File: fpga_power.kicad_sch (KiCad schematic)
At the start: 77 parts, among them U2 XC7A50T-FGG484, U3 LP3878MR-ADJ, U4 LP3878MR-ADJ, U5 LP3878MR-ADJ, U6 LP3878MR-ADJ, U7 LP3878MR-ADJ, U8 MCP23008-E/ML

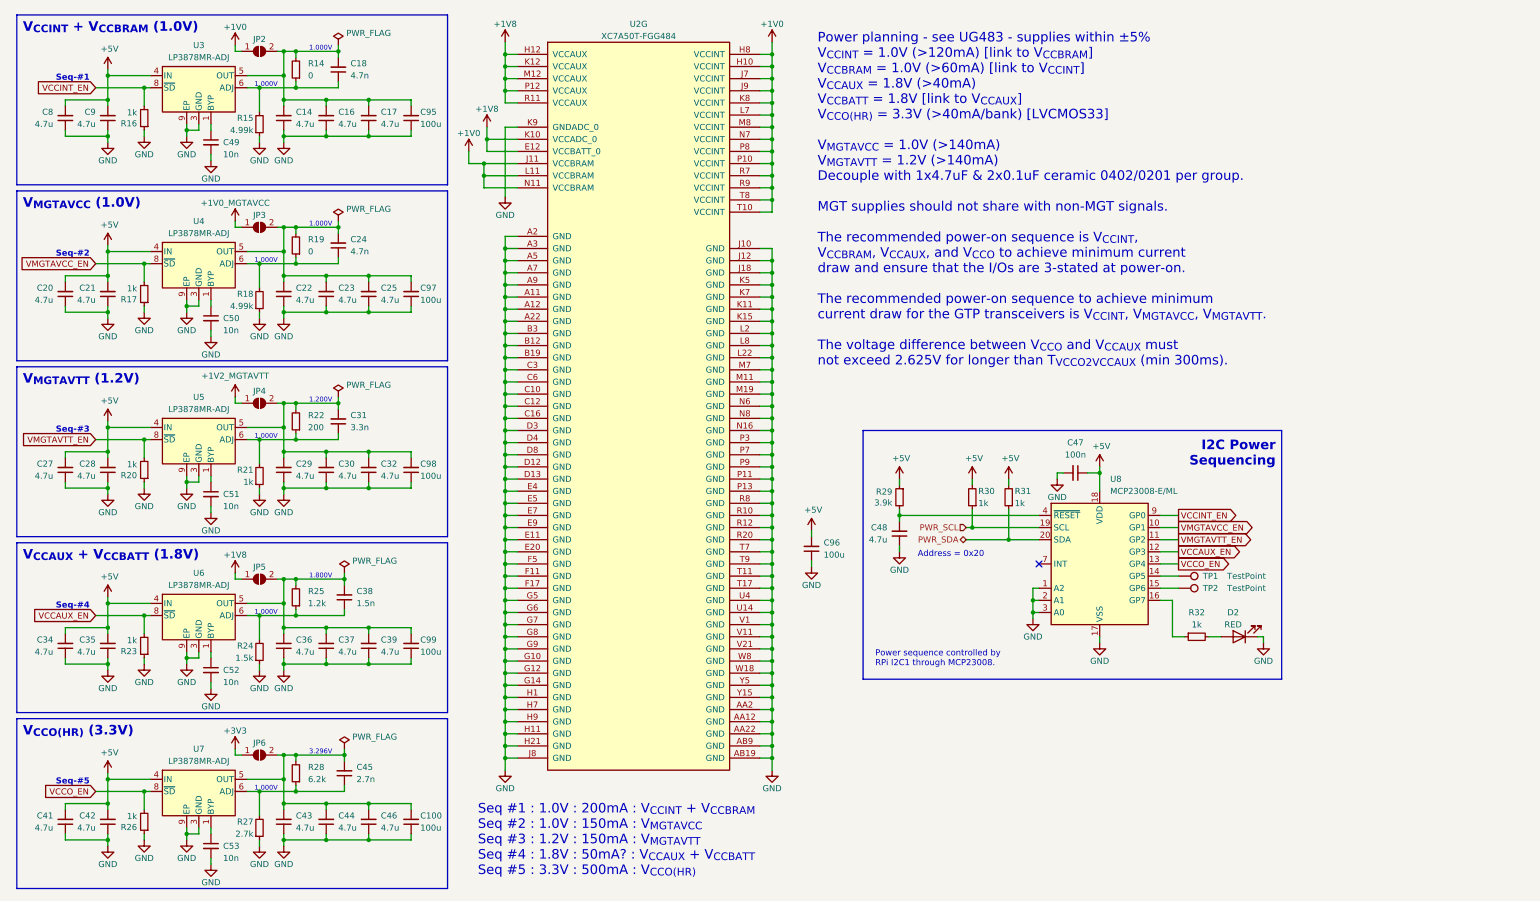
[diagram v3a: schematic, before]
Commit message: Changed linear PSU for SMPS and a few other changes
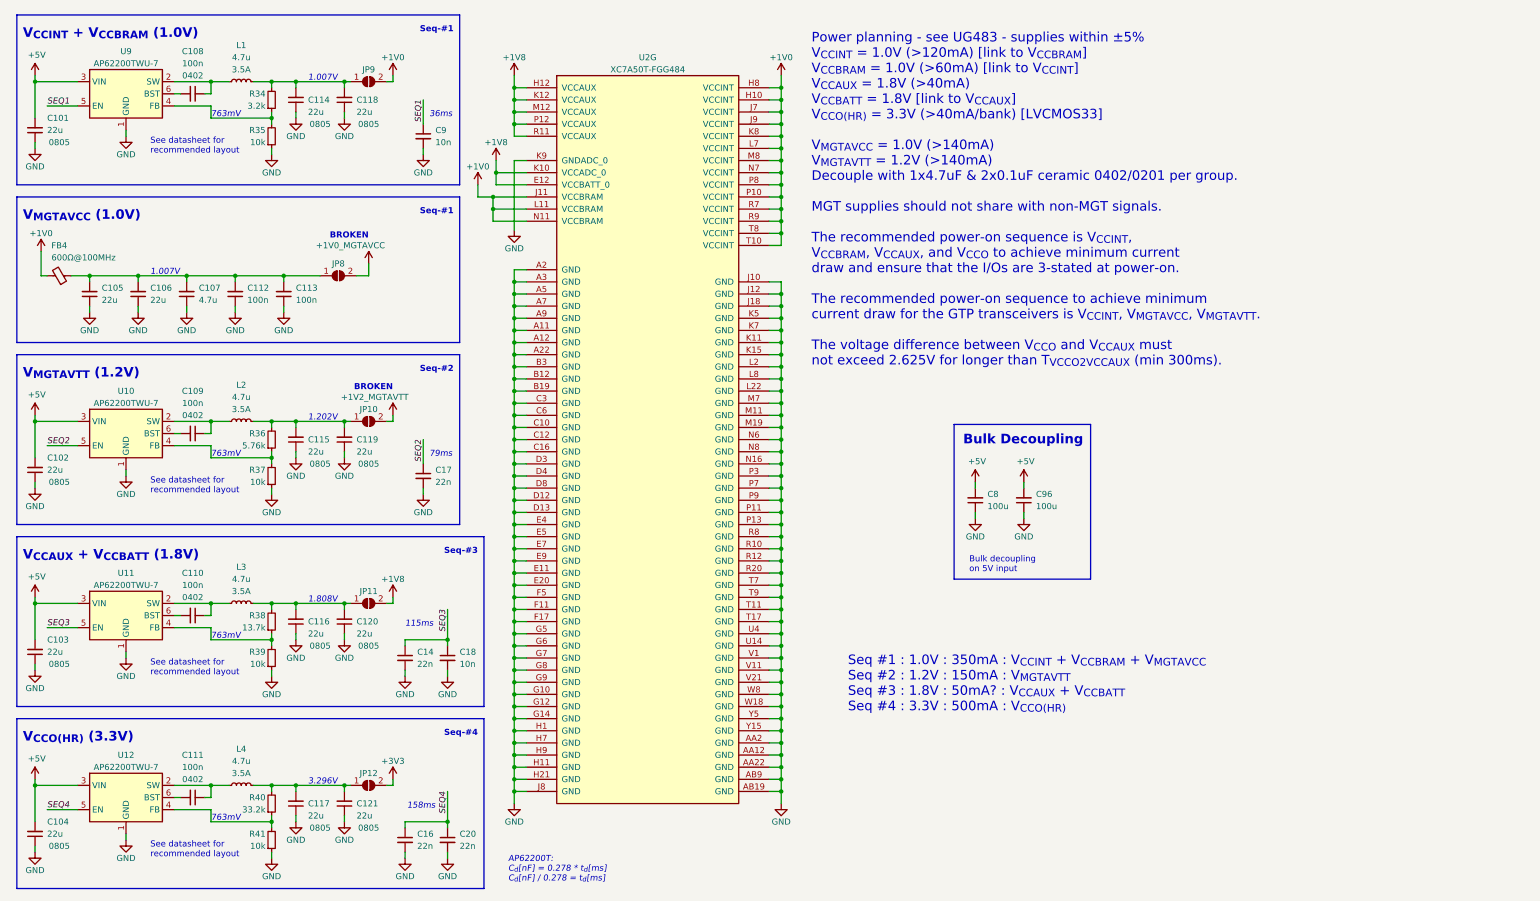
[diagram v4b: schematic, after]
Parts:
- removed C100, C95, C97, C98, C99: 100u, Capacitor_SMD:C_1206_3216Metric_Pad1.33x1.80mm_HandSolder, symbol Device:C_Small
- removed C21, C22, C23, C25, C27, C28, C29, C30, C32, C34, C35, C36, C37, C39, C41, C42, C43, C44, C46, C48: 4.7u, Capacitor_SMD:C_0402_1005Metric_Pad0.74x0.62mm_HandSolder, symbol Device:C_Small
- removed C24: 4.7n, Capacitor_SMD:C_0402_1005Metric_Pad0.74x0.62mm_HandSolder, symbol Device:C_Small
- removed C31: 3.3n, Capacitor_SMD:C_0402_1005Metric_Pad0.74x0.62mm_HandSolder, symbol Device:C_Small
- removed C38: 1.5n, Capacitor_SMD:C_0402_1005Metric_Pad0.74x0.62mm_HandSolder, symbol Device:C_Small
- removed C45: 2.7n, Capacitor_SMD:C_0402_1005Metric_Pad0.74x0.62mm_HandSolder, symbol Device:C_Small
- removed C47: 100n, Capacitor_SMD:C_0402_1005Metric_Pad0.74x0.62mm_HandSolder, symbol Device:C_Small
- removed C49, C50, C51, C52, C53: 10n, Capacitor_SMD:C_0402_1005Metric_Pad0.74x0.62mm_HandSolder, symbol Device:C_Small
- removed D2: RED, LED_SMD:LED_0603_1608Metric_Pad1.05x0.95mm_HandSolder, symbol Device:LED
- removed JP2, JP3, JP4, JP5, JP6: ID_WP, Jumper:SolderJumper-2_P1.3mm_Open_TrianglePad1.0x1.5mm, symbol Jumper:SolderJumper_2_Open
- removed R14, R19: 0, Resistor_SMD:R_0402_1005Metric_Pad0.72x0.64mm_HandSolder, symbol Device:R_Small
- removed R15, R18: 4.99k, Resistor_SMD:R_0402_1005Metric_Pad0.72x0.64mm_HandSolder, symbol Device:R_Small
- removed R16, R17, R20, R21, R23, R26, R30, R31, R32: 1k, Resistor_SMD:R_0402_1005Metric_Pad0.72x0.64mm_HandSolder, symbol Device:R_Small
- removed R22: 200, Resistor_SMD:R_0402_1005Metric_Pad0.72x0.64mm_HandSolder, symbol Device:R_Small
- removed R24: 1.5k, Resistor_SMD:R_0402_1005Metric_Pad0.72x0.64mm_HandSolder, symbol Device:R_Small
- removed R25: 1.2k, Resistor_SMD:R_0402_1005Metric_Pad0.72x0.64mm_HandSolder, symbol Device:R_Small
- removed R27: 2.7k, Resistor_SMD:R_0402_1005Metric_Pad0.72x0.64mm_HandSolder, symbol Device:R_Small
- removed R28: 6.2k, Resistor_SMD:R_0402_1005Metric_Pad0.72x0.64mm_HandSolder, symbol Device:R_Small
- removed R29: 3.9k, Resistor_SMD:R_0402_1005Metric_Pad0.72x0.64mm_HandSolder, symbol Device:R_Small
- removed TP1, TP2: TestPoint, TestPoint:TestPoint_Pad_D1.0mm, symbol Connector:TestPoint
- removed U3, U4, U5, U6, U7: LP3878MR-ADJ, Package_SO:TI_SO-PowerPAD-8, symbol LP3878SD-ADJ:LP3878SD-ADJ
- removed U8: MCP23008-E/ML, Package_DFN_QFN:QFN-20-1EP_4x4mm_P0.5mm_EP2.7x2.7mm, symbol Interface_Expansion:MCP23008-xML
- added C101, C102, C103, C104, C105, C106, C114, C115, C116, C117, C118, C119, C120, C121: 22u, Capacitor_SMD:C_0805_2012Metric, symbol Device:C_Small
- added C107: 4.7u, Capacitor_SMD:C_0402_1005Metric_Pad0.74x0.62mm_HandSolder, symbol Device:C_Small
- added C108, C109, C110, C111: 100n, Capacitor_SMD:C_0402_1005Metric, symbol Device:C_Small
- added C112, C113: 100n, Capacitor_SMD:C_0402_1005Metric_Pad0.74x0.62mm_HandSolder, symbol Device:C_Small
- added FB4: 600Ω@100MHz, Inductor_SMD:L_0603_1608Metric_Pad1.05x0.95mm_HandSolder, symbol Device:FerriteBead_Small
- added JP10, JP11, JP12, JP8, JP9: ID_WP, Jumper:SolderJumper-2_P1.3mm_Open_TrianglePad1.0x1.5mm, symbol Jumper:SolderJumper_2_Open
- added L1, L2, L3, L4: 4.7u, Inductor_SMD:L_Chilisin_BMRB00050518, symbol Device:L_Small
- added R34: 3.2k, Resistor_SMD:R_0402_1005Metric, symbol Device:R_Small
- added R35, R37, R39, R41: 10k, Resistor_SMD:R_0402_1005Metric, symbol Device:R_Small
- added R36: 5.76k, Resistor_SMD:R_0402_1005Metric, symbol Device:R_Small
- added R38: 13.7k, Resistor_SMD:R_0402_1005Metric, symbol Device:R_Small
- added R40: 33.2k, Resistor_SMD:R_0402_1005Metric, symbol Device:R_Small
- added U10, U11, U12, U9: AP62200TWU-7, Package_TO_SOT_SMD:TSOT-23-6, symbol Diodes-Incorporated-AP62200:AP62200TWU-7
- C14, C16, C17, C20: value 4.7u -> 22n; footprint Capacitor_SMD:C_0402_1005Metric_Pad0.74x0.62mm_HandSolder -> Capacitor_SMD:C_0402_1005Metric; LCSC C23733 -> C1532; Pkg (none) -> 0402
- C18: value 4.7n -> 10n; footprint Capacitor_SMD:C_0402_1005Metric_Pad0.74x0.62mm_HandSolder -> Capacitor_SMD:C_0402_1005Metric; LCSC C1538 -> C15195; Pkg (none) -> 0402
- C8: value 4.7u -> 100u; footprint Capacitor_SMD:C_0402_1005Metric_Pad0.74x0.62mm_HandSolder -> Capacitor_SMD:C_1206_3216Metric_Pad1.33x1.80mm_HandSolder; LCSC C23733 -> C15008
- C9: value 4.7u -> 10n; footprint Capacitor_SMD:C_0402_1005Metric_Pad0.74x0.62mm_HandSolder -> Capacitor_SMD:C_0402_1005Metric; LCSC C23733 -> C15195; Pkg (none) -> 0402
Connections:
- net +1V0: now also FB4.2, JP8.2 (B), JP9.2 (B)
- net +1V2: now also JP10.2 (B)
- net +1V8: now also JP11.2 (B)
- net +3V3: now also JP12.2 (B)
- net +5V: now also C101.2, C102.2, C103.2, C104.2, U10.3 (VIN), U11.3 (VIN), U12.3 (VIN), U9.3 (VIN); no longer C20.2, C9.2
- net GND: now also C14.2, C16.2, C17.2, C18.2, C20.2, C9.2, C101.1, C102.1, C103.1, C104.1, C105.1, C106.1, C107.1, C112.1, C113.1, C114.1, C115.1, C116.1, C117.1, C118.1, C119.1, C120.1, C121.1, R35.1, R37.1, R39.1, R41.1, U10.1 (GND), U11.1 (GND), U12.1 (GND), U9.1 (GND); no longer C14.1, C16.1, C17.1, C20.1, C9.1
- net SEQ3: now reaches C18.1
- net SEQ3: now also C14.1, U11.5 (EN)
- new net: R40.1, R41.2, U12.4 (FB)
- new net: C117.2, C121.2, JP12.1 (A), L4.2, R40.2
- new net: C105.2, C106.2, C107.2, C112.2, C113.2, FB4.1, JP8.1 (A)
- new net: C110.1, L3.1, U11.2 (SW)
- new net: C116.2, C120.2, JP11.1 (A), L3.2, R38.2
- new net: C114.2, C118.2, JP9.1 (A), L1.2, R34.2
- new net: C109.1, L2.1, U10.2 (SW)
- new net: R36.1, R37.2, U10.4 (FB)
- new net: C109.2, U10.6 (BST)
- new net: C115.2, C119.2, JP10.1 (A), L2.2, R36.2
- new net: C111.1, L4.1, U12.2 (SW)
- new net: C111.2, U12.6 (BST)
- new net: R34.1, R35.2, U9.4 (FB)
- new net: R38.1, R39.2, U11.4 (FB)
- new net: C108.1, L1.1, U9.2 (SW)
- new net: C108.2, U9.6 (BST)
- new net: C110.2, U11.6 (BST)
- new net SEQ1: C9.1, U9.5 (EN)
- new net SEQ2: C17.1, U10.5 (EN)
- new net SEQ4: C16.1, C20.1, U12.5 (EN)
- no-connect marks 1 -> 0
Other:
- note added: "1.007V"
- note added: "1.202V"
- note added: "1.808V"
- note added: "115ms"
- note added: "158ms"
- note added: "36ms"
- note added: "763mV"
- note added: "79ms"
- note added: "AP62200T: C_{d}[nF] = 0.278 * t_{d}[ms] C_{d}[nF] / 0.278 = t_{d}[ms]"
- note added: "BROKEN"
- note added: "Bulk Decoupling"
- note added: "Bulk decoupling on 5V input"
- note added: "See datasheet for recommended layout"
- note added: "Seq #1 : 1.0V : 350mA : V_{CCINT} + V_{CCBRAM} + V_{MGTAVCC} Seq #2 : 1.2V : 150mA : V_{MGTAVTT} Seq #3 : 1.8V : 50mA? : V_{CCAUX} + V_{CCBATT} Seq #4 : 3.3V : 500mA : V_{CCO(HR)}"
- note removed: "1.000V"
- note removed: "1.200V"
- note removed: "1.800V"
- note removed: "Address = 0x20"
- note removed: "I2C Power Sequencing"
- note removed: "Power sequence controlled by RPi I2C1 through MCP23008."
- note removed: "Seq #1 : 1.0V : 200mA : V_{CCINT} + V_{CCBRAM} Seq #2 : 1.0V : 150mA : V_{MGTAVCC} Seq #3 : 1.2V : 150mA : V_{MGTAVTT} Seq #4 : 1.8V : 50mA? : V_{CCAUX} + V_{CCBATT} Seq #5 : 3.3V : 500mA : V_{CCO(HR)}"
- note removed: "Seq-#5"
- moved on the sheet: C96, U2G

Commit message: More routing and tinkering. Need to do non-MGT decoupling next.
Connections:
- net +1V0: no longer JP8.2 (B)
- net 1V0_FB: now reaches C105.2, C106.2, C107.2, C112.2, C113.2, FB4.1, JP8.1 (A)
- net +1V2 renamed +1V2_MGTAVTT
- new net +1V0_MGTAVCC: JP8.2 (B)
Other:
- note removed: "BROKEN"
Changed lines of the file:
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@@
     (effects (font (size 2 2) (thickness 0.4) bold) (justify left bottom))
-  )
-  (text "BROKEN" (at 92.71 92.71 0)
-    (effects (font (size 1.27 1.27) (thickness 0.254) bold (color 255 0 0 1)) (justify right bottom))
   )
   (text "AP62200T:\nC_{d}[nF] = 0.278 * t_{d}[ms]\nC_{d}[nF] / 0.278 = t_{d}[ms]"
@@
     (effects (font (size 1.27 1.27) italic) (justify left bottom))
   )
-  (text "BROKEN" (at 87.63 60.96 0)
-    (effects (font (size 1.27 1.27) (thickness 0.254) bold (color 255 0 0 1)) (justify right bottom))
-  )
   (text "See datasheet for\nrecommended layout" (at 41.91 152.4 0)
     (effects (font (size 1.27 1.27)) (justify left bottom))
@@
   (label "SEQ2" (at 20.32 104.14 0) (fields_autoplaced)
     (effects (font (size 1.27 1.27) italic) (justify left bottom))
+  )
+  (label "1V0_FB" (at 60.96 68.58 0) (fields_autoplaced)
+    (effects (font (size 1.27 1.27)) (justify left bottom))
   )
   (label "SEQ1" (at 99.06 31.75 270) (fields_autoplaced)
@@
     )
   )
+  (symbol (lib_id "fpga_mgt_power:+1V2_MGTAVTT") (at 92.71 97.79 0) (unit 1)
+    (in_bom yes) (on_board yes) (dnp no)
+    (property "Reference" "#PWR037" (at 92.71 101.6 0)
+      (effects (font (size 1.27 1.27)) hide)
+    )
+    (property "Value" "+1V2_MGTAVTT" (at 92.71 93.98 0)
+      (effects (font (size 1.27 1.27)))
+    )
+    (property "Footprint" "" (at 92.71 97.79 0)
+      (effects (font (size 1.27 1.27)) hide)
+    )
+    (property "Datasheet" "" (at 92.71 97.79 0)
+      (effects (font (size 1.27 1.27)) hide)
+    )
+    (pin "1")
+    (instances
+      (project "Pi5-Artix50T-Hat"
+        (path "/e63e39d7-6ac0-4ffd-8aa3-1841a4541b55/58f29d61-b732-4149-afb6-3ea37966fd1b/2c454d17-99ad-41db-bad8-d6d4ac78a4ea"
+          (reference "#PWR037") (unit 1)
+        )
+      )
+    )
+  )
   (symbol (lib_id "power:GND") (at 82.55 106.68 0) (unit 1)
     (in_bom yes) (on_board yes) (dnp no)
@@
     )
   )
-  (symbol (lib_name "+1V0_1") (lib_id "power:+1V0") (at 87.63 66.04 0) (mirror y) (unit 1)
-    (in_bom yes) (on_board yes) (dnp no)
-    (property "Reference" "#PWR0172" (at 87.63 69.85 0)
-      (effects (font (size 1.27 1.27)) hide)
-    )
-    (property "Value" "+1V0_MGTAVCC" (at 83.82 62.23 0)
-      (effects (font (size 1.27 1.27)))
-    )
-    (property "Footprint" "" (at 87.63 66.04 0)
-      (effects (font (size 1.27 1.27)) hide)
-    )
-    (property "Datasheet" "" (at 87.63 66.04 0)
-      (effects (font (size 1.27 1.27)) hide)
-    )
-    (pin "1")
-    (instances
-      (project "Pi5-Artix50T-Hat"
-        (path "/e63e39d7-6ac0-4ffd-8aa3-1841a4541b55/58f29d61-b732-4149-afb6-3ea37966fd1b/2c454d17-99ad-41db-bad8-d6d4ac78a4ea"
-          (reference "#PWR0172") (unit 1)
-        )
-      )
-    )
-  )
   (symbol (lib_id "power:GND") (at 118.11 59.055 0) (unit 1)
     (in_bom yes) (on_board yes) (dnp no)
@@
     )
   )
+  (symbol (lib_id "fpga_mgt_power:+1V0_MGTAVCC") (at 87.63 66.04 0) (unit 1)
+    (in_bom yes) (on_board yes) (dnp no)
+    (property "Reference" "#PWR030" (at 87.63 69.85 0)
+      (effects (font (size 1.27 1.27)) hide)
+    )
+    (property "Value" "+1V0_MGTAVCC" (at 87.63 62.23 0)
+      (effects (font (size 1.27 1.27)))
+    )
+    (property "Footprint" "" (at 87.63 66.04 0)
+      (effects (font (size 1.27 1.27)) hide)
+    )
+    (property "Datasheet" "" (at 87.63 66.04 0)
+      (effects (font (size 1.27 1.27)) hide)
+    )
+    (pin "1")
+    (instances
+      (project "Pi5-Artix50T-Hat"
+        (path "/e63e39d7-6ac0-4ffd-8aa3-1841a4541b55/58f29d61-b732-4149-afb6-3ea37966fd1b/2c454d17-99ad-41db-bad8-d6d4ac78a4ea"
+          (reference "#PWR030") (unit 1)
+        )
+      )
+    )
+  )
   (symbol (lib_id "Device:C_Small") (at 50.8 30.48 270) (unit 1)
     (in_bom yes) (on_board yes) (dnp no)
@@
         )
       )
-    )
-  )
-  (symbol (lib_name "+1V2_1") (lib_id "power:+1V2") (at 92.71 97.79 0) (unit 1)
-    (in_bom yes) (on_board yes) (dnp no)
-    (property "Reference" "#PWR0174" (at 92.71 101.6 0)
-      (effects (font (size 1.27 1.27)) hide)
-    )
-    (property "Value" "+1V2_MGTAVTT" (at 88.9 93.98 0)
-      (effects (font (size 1.27 1.27)))
-    )
-    (property "Footprint" "" (at 92.71 97.79 0)
-      (effects (font (size 1.27 1.27)) hide)
-    )
-    (property "Datasheet" "" (at 92.71 97.79 0)
-      (effects (font (size 1.27 1.27)) hide)
-    )
-    (pin "1")
-    (instances
-      (project "Pi5-Artix50T-Hat"
-        (path "/e63e39d7-6ac0-4ffd-8aa3-1841a4541b55/58f29d61-b732-4149-afb6-3ea37966fd1b/2c454d17-99ad-41db-bad8-d6d4ac78a4ea"
-          (reference "#PWR0174") (unit 1)
-        )
-      )
